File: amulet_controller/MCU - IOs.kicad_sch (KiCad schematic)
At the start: 7 parts, among them U1 STM32G474RET3

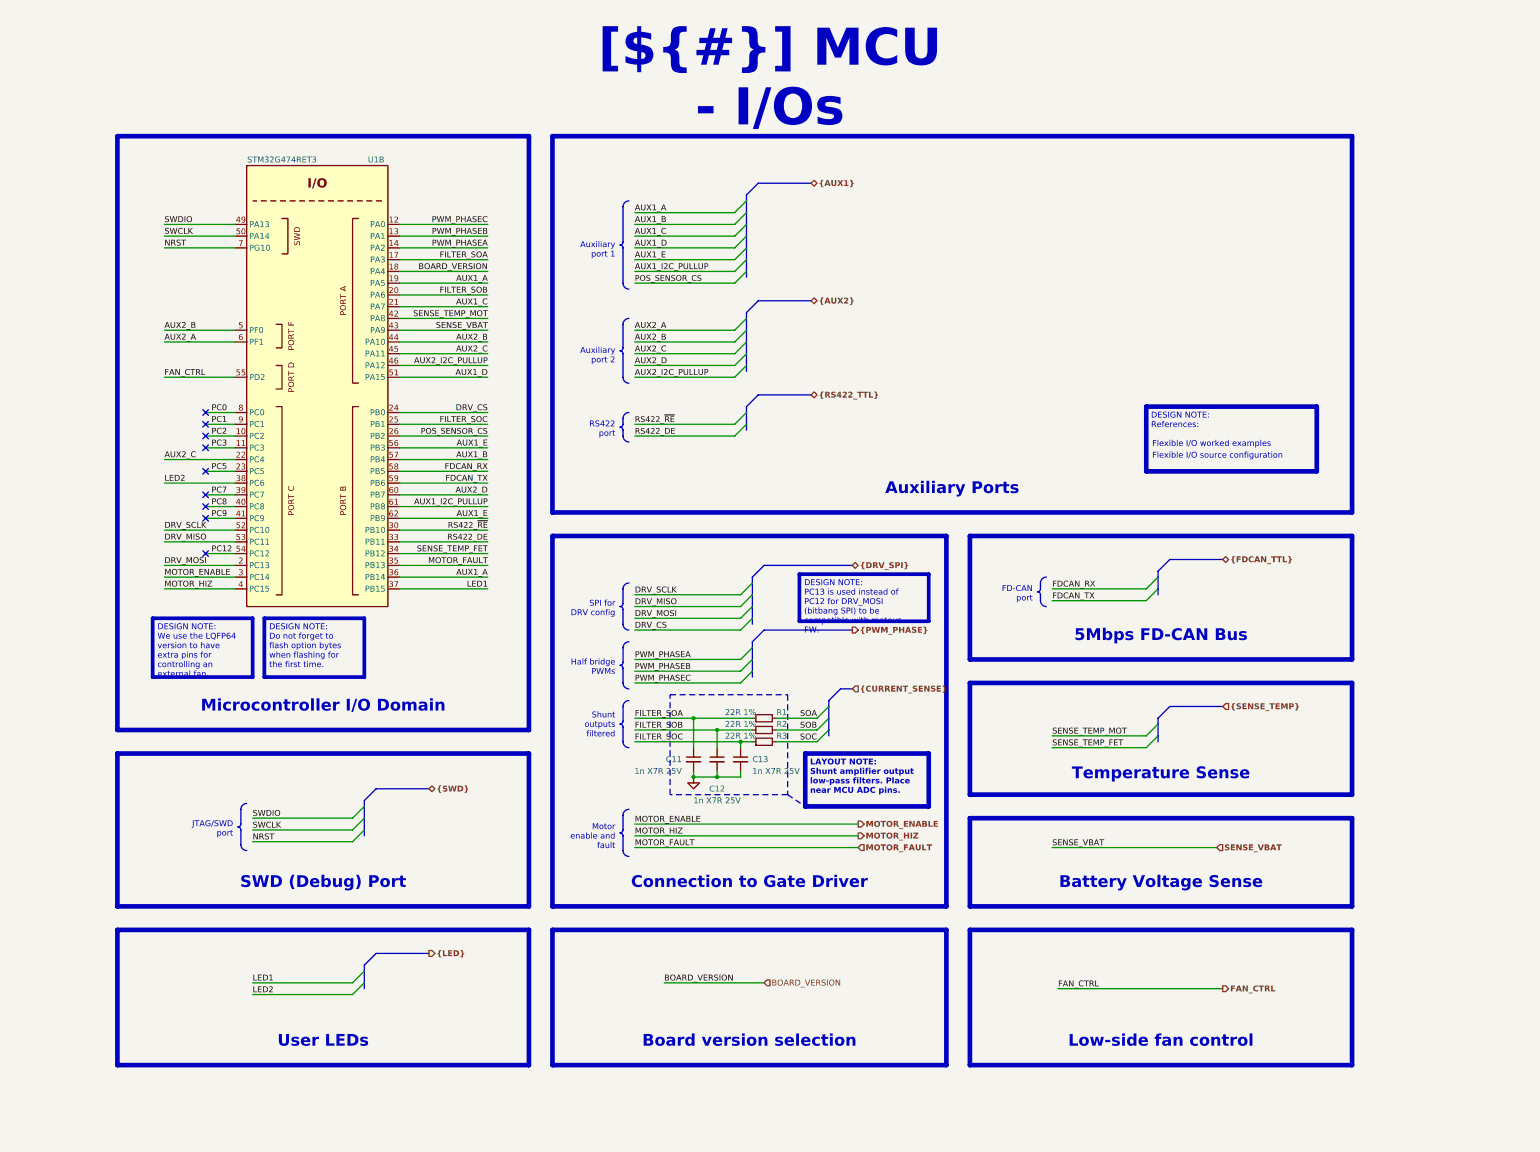
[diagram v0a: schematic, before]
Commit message: filled in fields for bom, replaced inexisting components. Need to replace LEDs
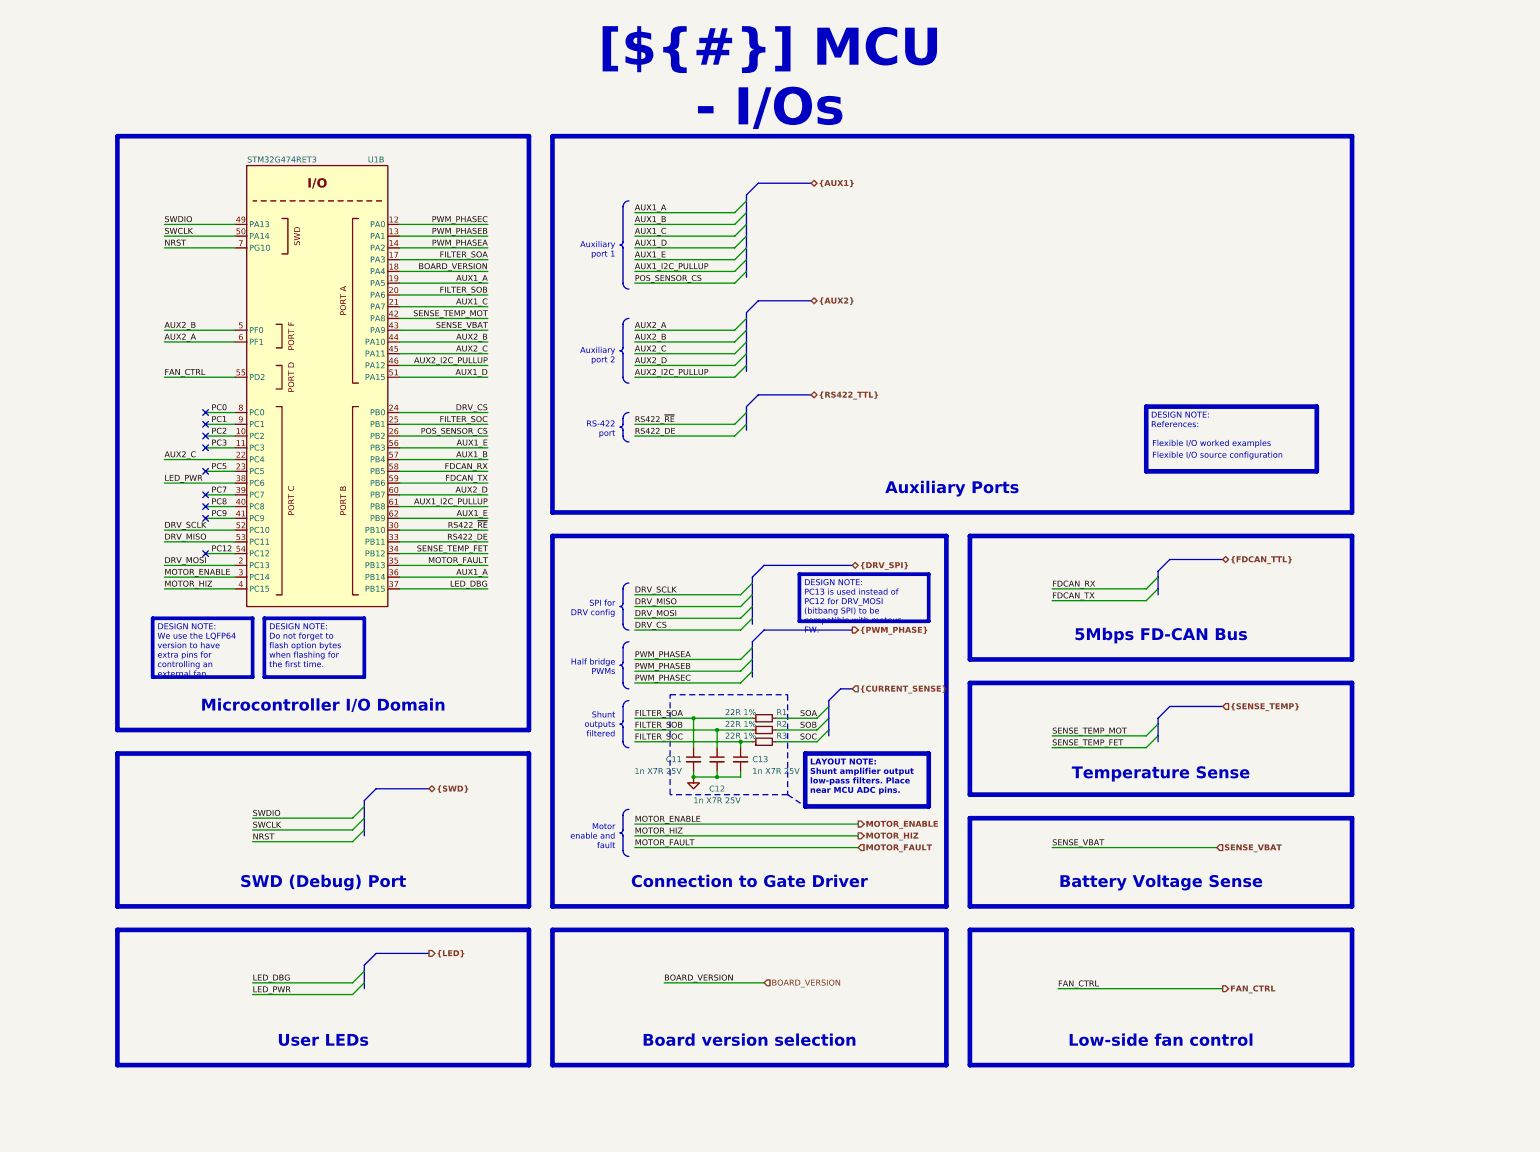
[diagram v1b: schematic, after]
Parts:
- C11, C12, C13: Manufacturer (none) -> YAGEO; Manufacturer Part Number (none) -> AC0402KRX7R8BB102; Supplier 1 (none) -> Digikey; Supplier Part Number 1 (none) -> 311-3065-1-ND
- R1, R2, R3: Manufacturer (none) -> Panasonic Electronic Components; Manufacturer Part Number (none) -> ERJ-2RKF22R0X; Supplier 1 (none) -> Digikey; Supplier Part Number 1 (none) -> P22.0LCT-ND
- U1: Manufacturer (none) -> STMicroelectronics; Manufacturer Part Number (none) -> STM32G474RET3; Supplier 1 (none) -> Digikey; Supplier Part Number 1 (none) -> 497-STM32G474RET3-ND
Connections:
- net LED1 renamed LED_DBG
- net LED2 renamed LED_PWR

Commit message: added test points
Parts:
- added TP1: MOTOR_ENABLE, 0_testpoint:TestPoint_Pad_D0.5mm_Front, symbol Connector:TestPoint
- added TP10: PWM_PHASEC, 0_testpoint:TestPoint_Pad_D0.5mm_Front, symbol Connector:TestPoint
- added TP11: SOA, 0_testpoint:TestPoint_Pad_D0.5mm_Front, symbol Connector:TestPoint
- added TP12: SOB, 0_testpoint:TestPoint_Pad_D0.5mm_Front, symbol Connector:TestPoint
- added TP13: SOC, 0_testpoint:TestPoint_Pad_D0.5mm_Front, symbol Connector:TestPoint
- added TP14: SWDIO, 0_testpoint:TestPoint_Pad_D0.5mm_Front, symbol Connector:TestPoint
- added TP15: SWCLK, 0_testpoint:TestPoint_Pad_D0.5mm_Front, symbol Connector:TestPoint
- added TP16: NRST, 0_testpoint:TestPoint_Pad_D0.5mm_Front, symbol Connector:TestPoint
- added TP17: AUX1_A, 0_testpoint:TestPoint_Pad_D0.5mm_Front, symbol Connector:TestPoint
- added TP18: AUX1_B, 0_testpoint:TestPoint_Pad_D0.5mm_Front, symbol Connector:TestPoint
- added TP19: AUX1_C, 0_testpoint:TestPoint_Pad_D0.5mm_Front, symbol Connector:TestPoint
- added TP2: MOTOR_HIZ, 0_testpoint:TestPoint_Pad_D0.5mm_Front, symbol Connector:TestPoint
- added TP20: AUX1_D, 0_testpoint:TestPoint_Pad_D0.5mm_Front, symbol Connector:TestPoint
- added TP21: AUX1_E, 0_testpoint:TestPoint_Pad_D0.5mm_Front, symbol Connector:TestPoint
- added TP22: AUX1_I2C_PULLUP, 0_testpoint:TestPoint_Pad_D0.5mm_Front, symbol Connector:TestPoint
- added TP23: POS_SENSOR_CS, 0_testpoint:TestPoint_Pad_D0.5mm_Back, symbol Connector:TestPoint
- added TP24: AUX2_A, 0_testpoint:TestPoint_Pad_D0.5mm_Front, symbol Connector:TestPoint
- added TP25: AUX2_B, 0_testpoint:TestPoint_Pad_D0.5mm_Front, symbol Connector:TestPoint
- added TP26: AUX2_C, 0_testpoint:TestPoint_Pad_D0.5mm_Front, symbol Connector:TestPoint
- added TP27: AUX2_D, 0_testpoint:TestPoint_Pad_D0.5mm_Front, symbol Connector:TestPoint
- added TP28: AUX2_I2C_PULLUP, 0_testpoint:TestPoint_Pad_D0.5mm_Front, symbol Connector:TestPoint
- added TP29: RS422_RE, 0_testpoint:TestPoint_Pad_D0.5mm_Back, symbol Connector:TestPoint
- added TP3: MOTOR_FAULT, 0_testpoint:TestPoint_Pad_D0.5mm_Front, symbol Connector:TestPoint
- added TP30: RS422_DE, 0_testpoint:TestPoint_Pad_D0.5mm_Back, symbol Connector:TestPoint
- added TP31: LED_DBG, 0_testpoint:TestPoint_Pad_D0.5mm_Front, symbol Connector:TestPoint
- added TP32: LED_PWR, 0_testpoint:TestPoint_Pad_D0.5mm_Front, symbol Connector:TestPoint
- added TP33: FD_CAN_RX, 0_testpoint:TestPoint_Pad_D0.5mm_Front, symbol Connector:TestPoint
- added TP34: FDCAN_TX, 0_testpoint:TestPoint_Pad_D0.5mm_Front, symbol Connector:TestPoint
- added TP35: FAN_CTRL, 0_testpoint:TestPoint_Pad_D0.5mm_Back, symbol Connector:TestPoint
- added TP36: SENSE_TEMP_MOT, 0_testpoint:TestPoint_Pad_D0.5mm_Back, symbol Connector:TestPoint
- added TP37: SENSE_TEMP_FET, 0_testpoint:TestPoint_Pad_D0.5mm_Front, symbol Connector:TestPoint
- added TP38: SENSE_VBAT, 0_testpoint:TestPoint_Pad_D0.5mm_Front, symbol Connector:TestPoint
- added TP4: DRV_SCLK, 0_testpoint:TestPoint_Pad_D0.5mm_Front, symbol Connector:TestPoint
- added TP5: DRV_MISO, 0_testpoint:TestPoint_Pad_D0.5mm_Front, symbol Connector:TestPoint
- added TP6: DRV_MOSI, 0_testpoint:TestPoint_Pad_D0.5mm_Front, symbol Connector:TestPoint
- added TP7: DRV_CS, 0_testpoint:TestPoint_Pad_D0.5mm_Back, symbol Connector:TestPoint
- added TP8: PWM_PHASEA, 0_testpoint:TestPoint_Pad_D0.5mm_Front, symbol Connector:TestPoint
- added TP9: PWM_PHASEB, 0_testpoint:TestPoint_Pad_D0.5mm_Front, symbol Connector:TestPoint
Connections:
- net AUX1_A: now also TP17.1
- net AUX1_B: now also TP18.1
- net AUX1_C: now also TP19.1
- net AUX1_D: now also TP20.1
- net AUX1_E: now also TP21.1
- net AUX1_I2C_PULLUP: now also TP22.1
- net AUX2_A: now also TP24.1
- net AUX2_B: now also TP25.1
- net AUX2_C: now also TP26.1
- net AUX2_D: now also TP27.1
- net AUX2_I2C_PULLUP: now also TP28.1
- net DRV_CS: now also TP7.1
- net DRV_MISO: now also TP5.1
- net DRV_MOSI: now also TP6.1
- net DRV_SCLK: now also TP4.1
- net FAN_CTRL: now also TP35.1
- net FDCAN_RX: now also TP33.1
- net FDCAN_TX: now also TP34.1
- net LED_DBG: now also TP31.1
- net LED_PWR: now also TP32.1
- net MOTOR_ENABLE: now also TP1.1
- net MOTOR_FAULT: now also TP3.1
- net MOTOR_HIZ: now also TP2.1
- net NRST: now also TP16.1
- net POS_SENSOR_CS: now also TP23.1
- net PWM_PHASEA: now also TP8.1
- net PWM_PHASEB: now also TP9.1
- net PWM_PHASEC: now also TP10.1
- net RS422_DE: now also TP30.1
- net RS422_~{RE}: now also TP29.1
- net SENSE_TEMP_FET: now also TP37.1
- net SENSE_TEMP_MOT: now also TP36.1
- net SENSE_VBAT: now also TP38.1
- net SOA: now also TP11.1
- net SOB: now also TP12.1
- net SOC: now also TP13.1
- net SWCLK: now also TP15.1
- net SWDIO: now also TP14.1
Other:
- moved on the sheet: C11, C12, C13, R1, R2, R3, U1B
